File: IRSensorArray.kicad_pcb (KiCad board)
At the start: 2 copper layers, 45 parts, among them J1 EXT_REF, J2 INPUT, J3 PASSTHRU, Q1 DETECT_0, Q2 DETECT_0, Q3 DETECT_0, Q4 DETECT_0, Q5 DETECT_0, Q6 DETECT_0, Q7 DETECT_0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

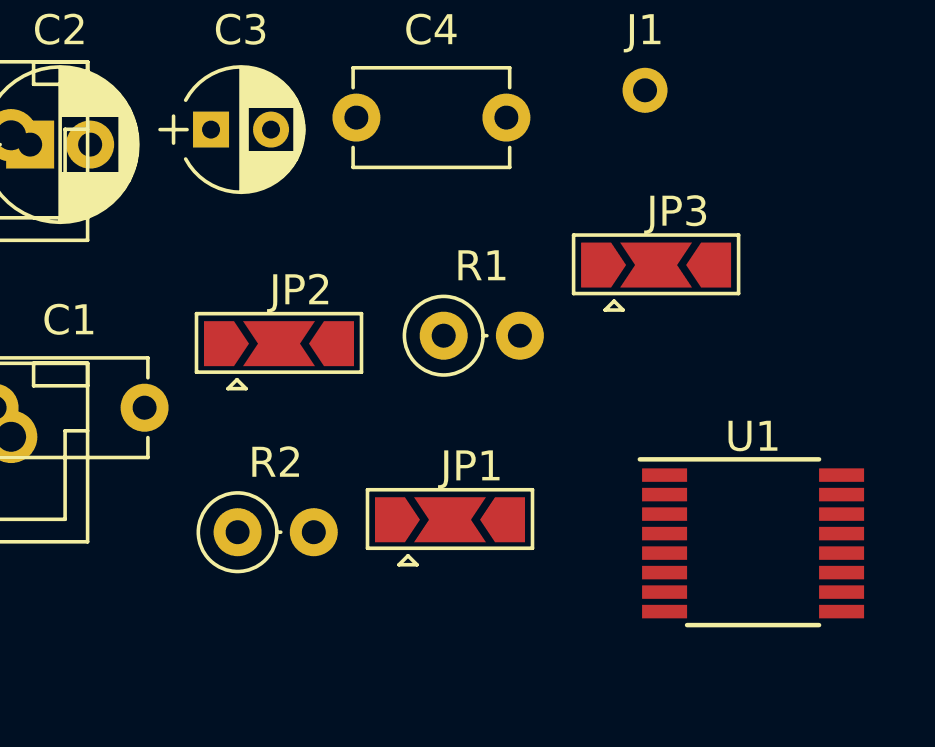
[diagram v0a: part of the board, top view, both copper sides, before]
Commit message: Changed triangle solder bridges to semi-circle
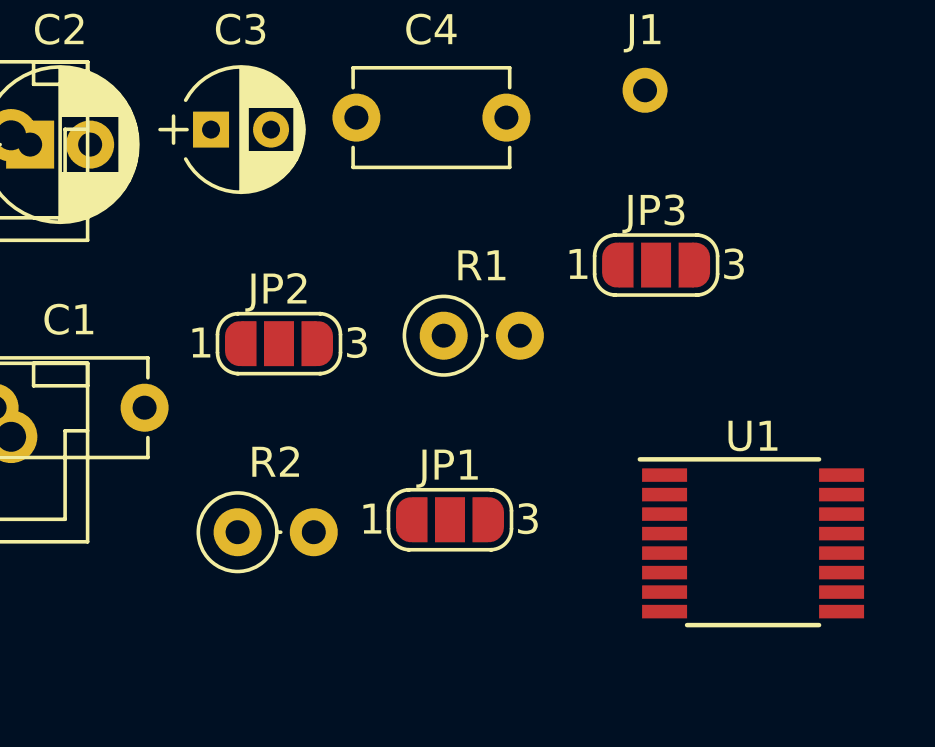
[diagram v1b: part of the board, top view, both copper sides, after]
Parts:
- JP1, JP2, JP3: footprint footprints:SolderJumper-3_P2.0mm_Open_TrianglePad1.0x1.5mm -> footprints:SolderJumper-3_P1.3mm_Open_RoundedPad1.0x1.5mm_NumberLabels

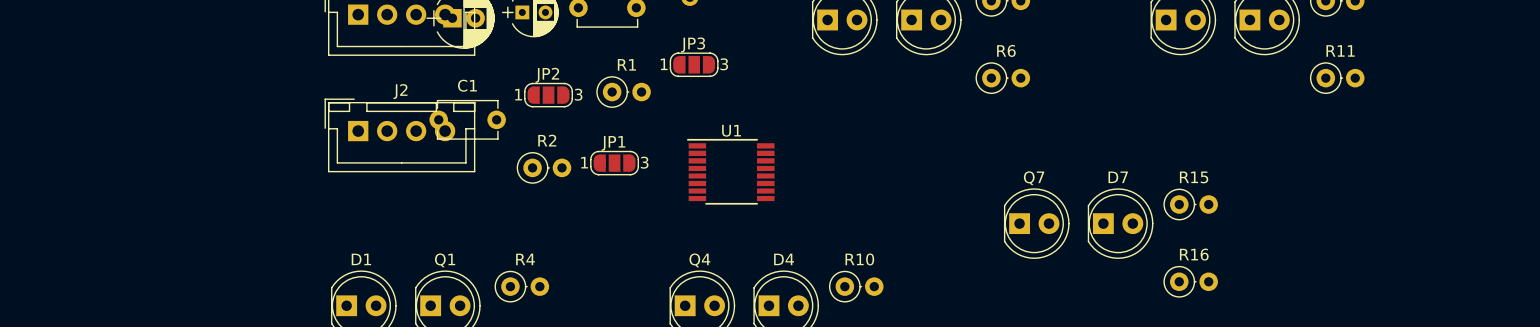
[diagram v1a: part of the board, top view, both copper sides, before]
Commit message: Added mounting holes and some fixes
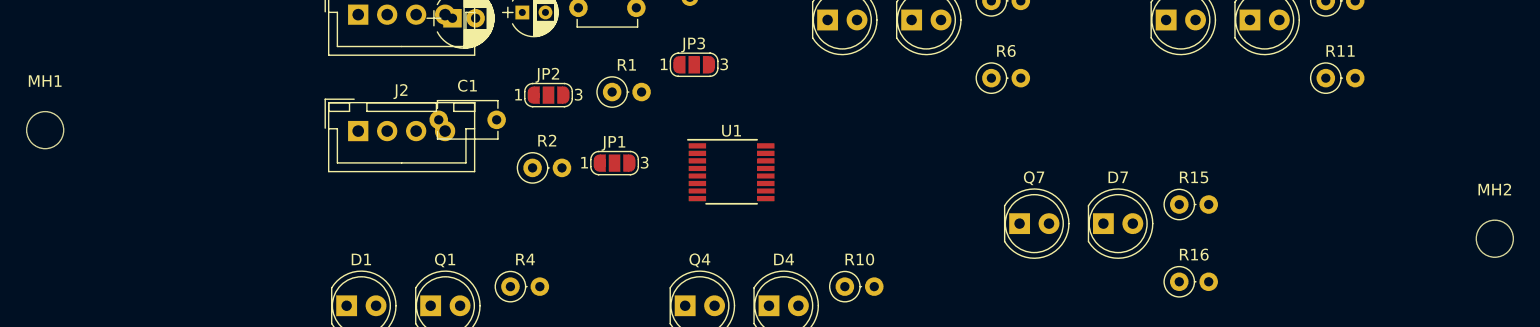
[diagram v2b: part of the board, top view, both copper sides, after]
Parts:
- added MH1: MountingHole_3.2mm_M3, Mounting_Holes:MountingHole_3.2mm_M3, F.Cu at (82.4, 79.9)
- added MH2: MountingHole_3.2mm_M3, Mounting_Holes:MountingHole_3.2mm_M3, F.Cu at (207.5, 89.3)
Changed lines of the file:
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@@
     (tracks 0)
     (zones 0)
-    (modules 45)
+    (modules 47)
     (nets 25)
   )
@@
     (add_net "Net-(D8-Pad2)")
     (add_net "Net-(J1-Pad1)")
+  )
+  (module Mounting_Holes:MountingHole_3.2mm_M3 locked (layer F.Cu)
+    (at 207.518 89.2556)
+    (descr "Mounting Hole 3.2mm, no annular, M3")
+    (tags "mounting hole 3.2mm no annular m3")
+    (attr virtual)
+    (fp_text reference MH2 (at 0 -4.2) (layer F.SilkS)
+      (effects (font (size 1 1) (thickness 0.15)))
+    )
+    (fp_text value MountingHole_3.2mm_M3 (at 0 4.2) (layer F.Fab)
+      (effects (font (size 1 1) (thickness 0.15)))
+    )
+    (fp_circle (center 0 0) (end 3.45 0) (layer F.CrtYd) (width 0.05))
+    (fp_circle (center 0 0) (end 3.2 0) (layer Cmts.User) (width 0.15))
+    (fp_text user %R (at 0.3 0) (layer F.Fab)
+      (effects (font (size 1 1) (thickness 0.15)))
+    )
+    (pad 1 np_thru_hole circle (at 0 0) (size 3.2 3.2) (drill 3.2) (layers *.Cu *.Mask))
   )
   (module Capacitors_THT:C_Disc_D5.1mm_W3.2mm_P5.00mm (layer F.Cu)
@@
       (net 3 +5V))
   )
+  (module Mounting_Holes:MountingHole_3.2mm_M3 locked (layer F.Cu)
+    (at 82.3722 79.883)
+    (descr "Mounting Hole 3.2mm, no annular, M3")
+    (tags "mounting hole 3.2mm no annular m3")
+    (attr virtual)
+    (fp_text reference MH1 (at 0 -4.2) (layer F.SilkS)
+      (effects (font (size 1 1) (thickness 0.15)))
+    )
+    (fp_text value MountingHole_3.2mm_M3 (at 0 4.2) (layer F.Fab)
+      (effects (font (size 1 1) (thickness 0.15)))
+    )
+    (fp_text user %R (at 0.3 0) (layer F.Fab)
+      (effects (font (size 1 1) (thickness 0.15)))
+    )
+    (fp_circle (center 0 0) (end 3.2 0) (layer Cmts.User) (width 0.15))
+    (fp_circle (center 0 0) (end 3.45 0) (layer F.CrtYd) (width 0.05))
+    (pad 1 np_thru_hole circle (at 0 0) (size 3.2 3.2) (drill 3.2) (layers *.Cu *.Mask))
+  )
 )

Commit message: Started PCB layout
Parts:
- Q1, Q2, Q3, Q4, Q5, Q6, Q7, Q8: value DETECT_0 -> DETECT
- moved D1 108.7 mm to (216.9, 102.2)
- moved Q1 108.7 mm to (224.1, 102.2)
- moved R3 108.7 mm to (231.0, 107.2)
- moved R4 108.7 mm to (231.0, 100.5)
- moved R5 98.9 mm to (70.3, 100.2)
- moved R6 98.9 mm to (70.3, 106.9)
- moved D2 98.9 mm to (56.2, 101.9)
- moved Q2 98.9 mm to (63.4, 101.9)
- moved D4 58.7 mm to (86.6, 102.1)
- moved Q4 58.3 mm to (79.7, 102.2)
- moved R10 58.3 mm to (93.5, 100.5)
- moved R9 58.3 mm to (93.5, 107.2)
- moved Q5 35.6 mm to (195.1, 102.1)
- moved R11 35.6 mm to (208.9, 107.1)
- moved R12 35.6 mm to (208.9, 100.5)
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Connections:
- Q1 pad 1: /CH0 -> GND
- Q1 pad 2: GND -> /CH0
- Q2 pad 1: /CH4 -> GND
- Q2 pad 2: GND -> /CH4
- Q3 pad 1: /CH1 -> GND
- Q3 pad 2: GND -> /CH1
- Q4 pad 1: /CH5 -> GND
- Q4 pad 2: GND -> /CH5
- Q5 pad 1: /CH2 -> GND
- Q5 pad 2: GND -> /CH2
- Q6 pad 1: /CH6 -> GND
- Q6 pad 2: GND -> /CH6
- Q7 pad 1: /CH3 -> GND
- Q7 pad 2: GND -> /CH3
- Q8 pad 1: /CH7 -> GND
- Q8 pad 2: GND -> /CH7

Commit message: First draft finished!
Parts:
- removed C3: 1uF, Capacitors_THT:CP_Radial_D4.0mm_P2.00mm
- added G***: LOGO, footprints:rover, B.Cu at (108.2, 127.8)
- J2, J3: moved to B.Cu
- moved R3 122.7 mm to (112.5, 139.2), turned to 90 degrees
- moved R4 122.5 mm to (112.5, 131.6), turned to 270 degrees
- moved Q1 121.7 mm to (106.2, 132.1)
- moved D1 116.6 mm to (106.2, 138.7)
- moved D2 97.8 mm to (146.8, 138.7)
- moved R5 91.5 mm to (153.2, 139.2), turned to 90 degrees
- moved Q2 88.7 mm to (146.8, 132.1)
- moved R6 86.4 mm to (153.2, 131.6), turned to 270 degrees
- moved D5 84.2 mm to (126.5, 138.7)
- moved Q4 82.9 mm to (157.0, 132.1)
- moved R11 82.6 mm to (132.8, 139.2), turned to 90 degrees
- moved R12 82.2 mm to (132.8, 131.6), turned to 270 degrees
- moved D4 79.3 mm to (157.0, 138.7)
- moved R9 76.8 mm to (163.3, 139.2), turned to 90 degrees
- moved R10 76.4 mm to (163.3, 131.6), turned to 270 degrees
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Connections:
- J2 pad 2: /SDA -> /SCL
- J2 pad 3: /SCL -> /SDA
- J3 pad 2: /SDA -> /SCL
- J3 pad 3: /SCL -> /SDA
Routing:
- net +5V: track 0.00 -> 172.3 mm, vias 0 -> 1
- net /SCL: track 0.00 -> 69.1 mm
- net /CH0: track 0.00 -> 56.8 mm
- net /SDA: track 0.00 -> 51.4 mm
- net /CH1: track 0.00 -> 47.9 mm
- net /CH2: track 0.00 -> 38.7 mm
- net /CH3: track 0.00 -> 29.5 mm
- net /CH4: track 0.00 -> 20.2 mm
- net /CH7: track 0.00 -> 18.1 mm
- net /REF: track 0.00 -> 11.3 mm
- net /CH5: track 0.00 -> 11.2 mm
- net /CH6: track 0.00 -> 10.2 mm
- net /SB_0: track 0.00 -> 9.68 mm
- net GND: track 0.00 -> 9.22 mm, vias 0 -> 3
- net /SB_1: track 0.00 -> 8.42 mm
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- added copper zone on B.Cu, net GND
- added copper zone on F.Cu, net GND
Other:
- board outline added: 82.8 x 25.4 mm
- board text added: "EXT_5V"
- board text added: "GND SDA SCL +5V"
- board text added: "INPUT / DAISY-CHAIN"
- board text added: "IR Sensor Array By V2FC"
- board text added: "IREF"
- board text added: "SB0"
- board text added: "SB1"

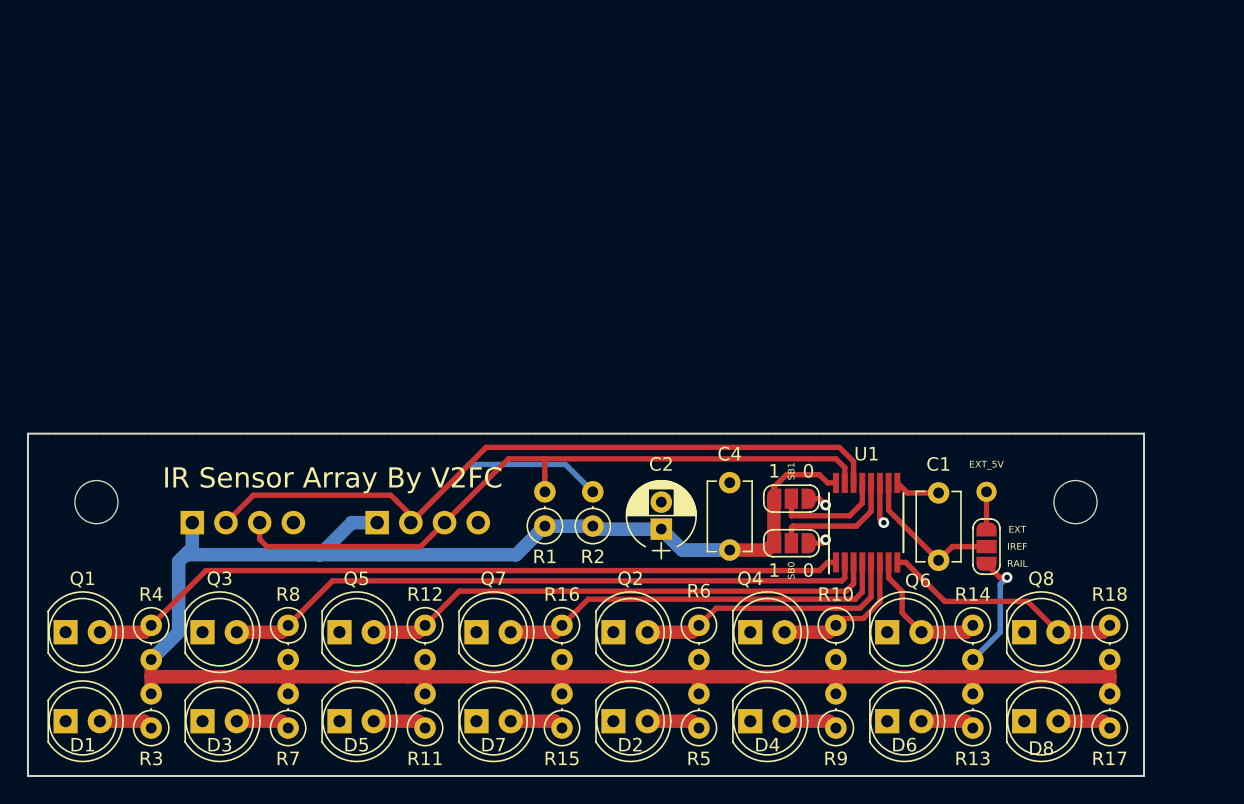
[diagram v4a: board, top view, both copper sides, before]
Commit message: Added images
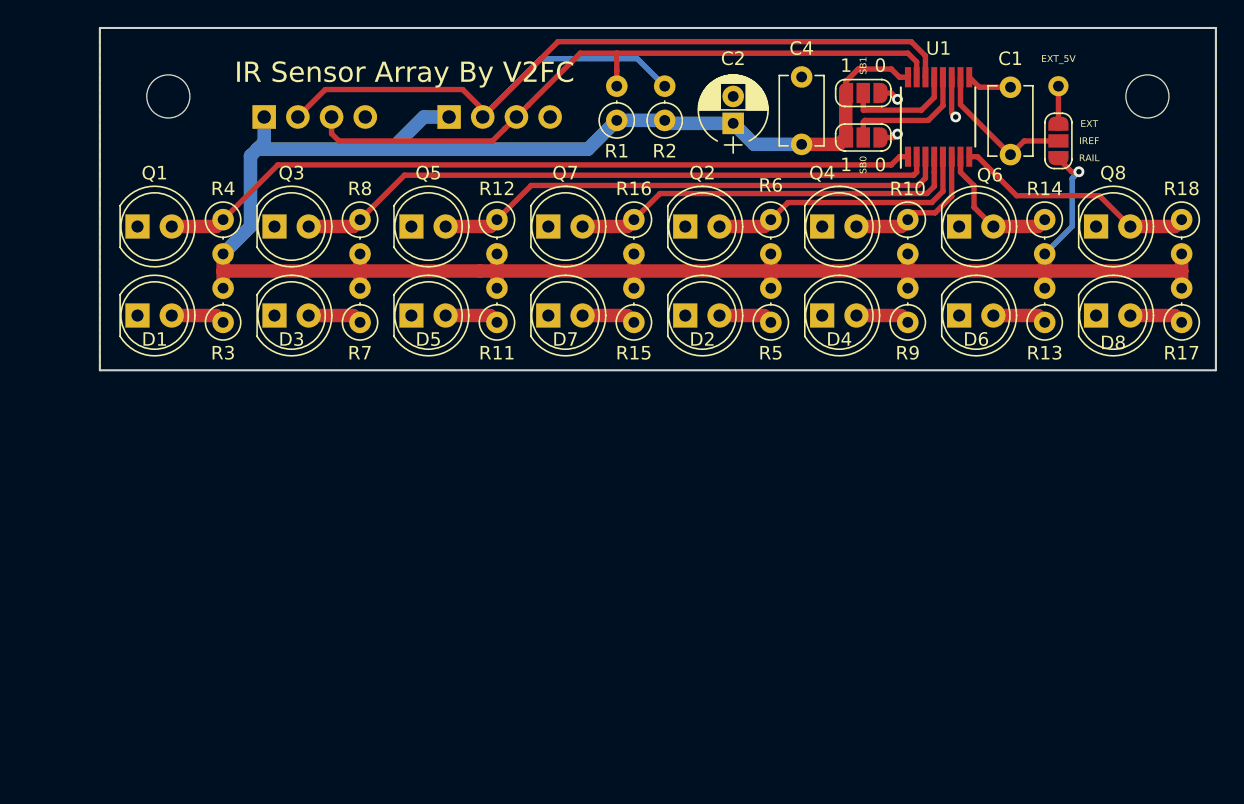
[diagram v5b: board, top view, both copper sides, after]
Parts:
- moved Q1 30.6 mm to (111.5, 102.0)
- moved Q3 30.6 mm to (121.7, 102.0)
- moved Q4 30.6 mm to (162.3, 102.0)
- moved Q5 30.6 mm to (131.8, 102.0)
- moved Q6 30.6 mm to (172.5, 102.0)
- moved Q7 30.6 mm to (142.0, 102.0)
- moved Q8 30.6 mm to (182.6, 102.0)
- moved Q2 30.6 mm to (152.1, 102.0)
- moved C2 30.6 mm to (155.7, 94.3)
- moved D1 30.6 mm to (111.5, 108.6)
- moved D3 30.6 mm to (121.7, 108.6)
- moved D4 30.6 mm to (162.3, 108.6)
- moved D5 30.6 mm to (131.8, 108.6)
- moved D6 30.6 mm to (172.5, 108.6)
- moved D7 30.6 mm to (142.0, 108.6)
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
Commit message: Added library for sensor
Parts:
- Q1, Q2, Q3, Q4, Q5, Q6, Q7, Q8: value DETECT -> QSD124
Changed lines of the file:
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@@
       (outputformat 1)
       (mirror false)
-      (drillshape 1)
+      (drillshape 0)
       (scaleselection 1)
       (outputdirectory ""))
@@
       (effects (font (size 1 1) (thickness 0.15)))
     )
-    (fp_text value DETECT (at 1.27 3.96) (layer F.Fab)
+    (fp_text value QSD124 (at 1.27 3.96) (layer F.Fab)
       (effects (font (size 1 1) (thickness 0.15)))
     )
@@
       (effects (font (size 1 1) (thickness 0.15)))
     )
-    (fp_text value DETECT (at 1.27 3.96) (layer F.Fab)
+    (fp_text value QSD124 (at 1.27 3.96) (layer F.Fab)
       (effects (font (size 1 1) (thickness 0.15)))
     )
@@
       (effects (font (size 1 1) (thickness 0.15)))
     )
-    (fp_text value DETECT (at 1.27 3.96) (layer F.Fab)
+    (fp_text value QSD124 (at 1.27 3.96) (layer F.Fab)
       (effects (font (size 1 1) (thickness 0.15)))
     )
@@
       (effects (font (size 1 1) (thickness 0.15)))
     )
-    (fp_text value DETECT (at 1.27 3.96) (layer F.Fab)
+    (fp_text value QSD124 (at 1.27 3.96) (layer F.Fab)
       (effects (font (size 1 1) (thickness 0.15)))
     )
@@
       (effects (font (size 1 1) (thickness 0.15)))
     )
-    (fp_text value DETECT (at 1.27 3.96) (layer F.Fab)
+    (fp_text value QSD124 (at 1.27 3.96) (layer F.Fab)
       (effects (font (size 1 1) (thickness 0.15)))
     )
@@
       (effects (font (size 1 1) (thickness 0.15)))
     )
-    (fp_text value DETECT (at 1.27 3.96) (layer F.Fab)
+    (fp_text value QSD124 (at 1.27 3.96) (layer F.Fab)
       (effects (font (size 1 1) (thickness 0.15)))
     )
@@
       (effects (font (size 1 1) (thickness 0.15)))
     )
-    (fp_text value DETECT (at 1.27 3.96) (layer F.Fab)
+    (fp_text value QSD124 (at 1.27 3.96) (layer F.Fab)
       (effects (font (size 1 1) (thickness 0.15)))
     )
@@
       (effects (font (size 1 1) (thickness 0.15)))
     )
-    (fp_text value DETECT (at 1.27 3.96) (layer F.Fab)
-      (effects (font (size 1 1) (thickness 0.15)))
-    )
+    (fp_text value QSD124 (at 1.27 3.96) (layer F.Fab)
+      (effects (font (size 1 1) (thickness 0.15)))
+    )

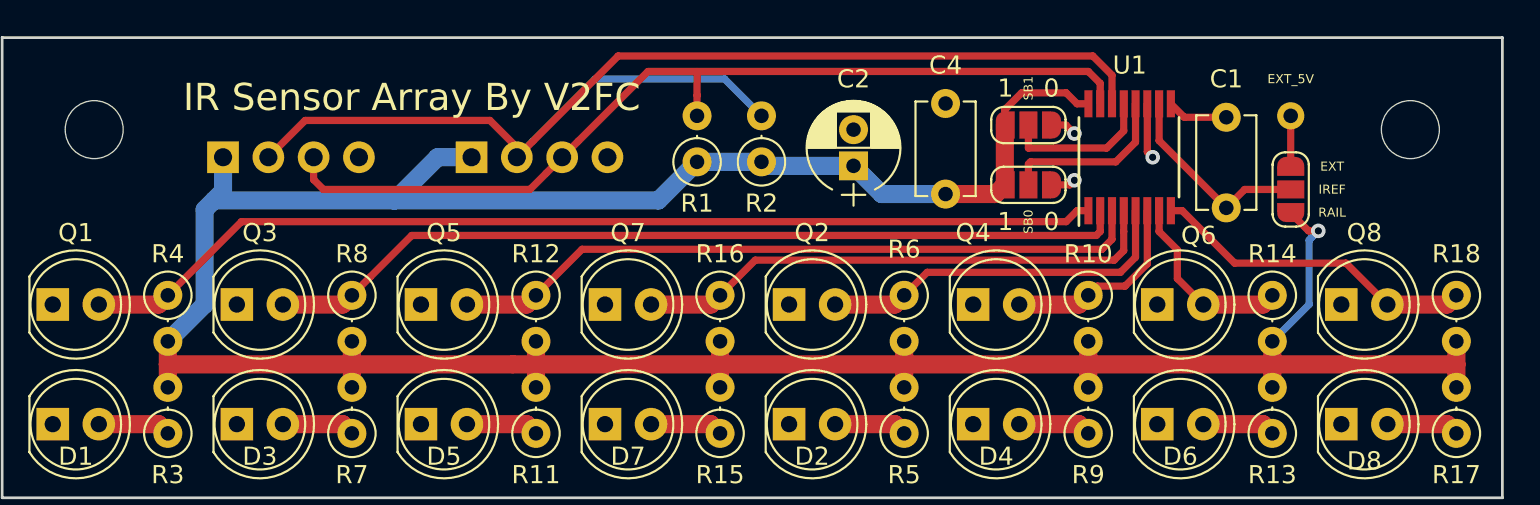
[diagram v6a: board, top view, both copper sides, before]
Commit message: Added reverse voltage diode
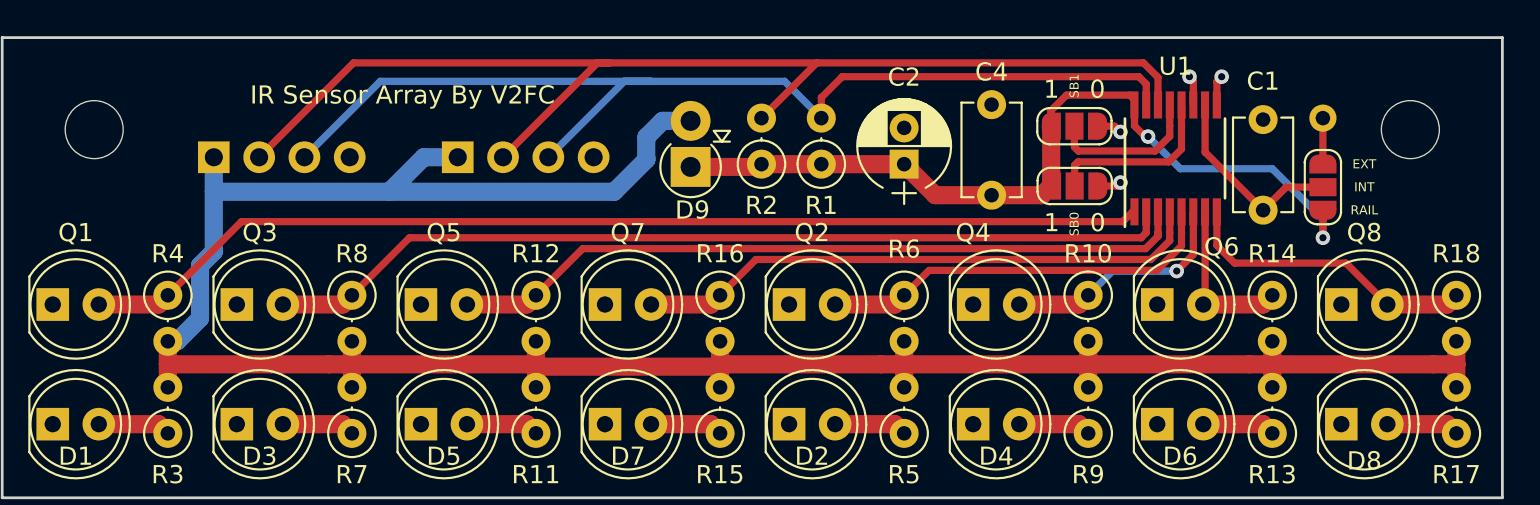
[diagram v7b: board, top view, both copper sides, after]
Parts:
- added D9: 1N4007, Diodes_THT:D_DO-41_SOD81_P2.54mm_Vertical_AnodeUp, F.Cu at (146.7, 94.4)
- D1, D2, D3, D4, D5, D6, D7, D8: value EMITTER -> HSDL-4420
- moved R1 6.86 mm to (153.9, 94.2)
- moved C2 2.80 mm to (158.5, 94.2)
- moved JP1 2.56 mm to (167.9, 95.4)
- moved U1 2.54 mm to (173.5, 93.9)
- moved C4 2.54 mm to (163.3, 95.9)
- moved JP3 2.54 mm to (167.9, 92.1)
- moved C1 2.04 mm to (178.3, 96.8)
- moved J1 1.78 mm to (181.6, 91.7)
- moved JP2 1.78 mm to (181.6, 95.5)
- moved J2 0.76 mm to (133.9, 93.9)
- moved J3 0.51 mm to (120.4, 93.9)
- moved R2 0.13 mm to (150.6, 94.2)
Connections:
- J2 pad 1: +5V -> VCC
- J3 pad 1: +5V -> VCC
- R10 pad 2: +5V -> VCC
- R11 pad 2: +5V -> VCC
- R12 pad 2: +5V -> VCC
- R13 pad 2: +5V -> VCC
- R14 pad 2: +5V -> VCC
- R15 pad 2: +5V -> VCC
- R16 pad 2: +5V -> VCC
- R17 pad 2: +5V -> VCC
- R18 pad 2: +5V -> VCC
- R3 pad 2: +5V -> VCC
- R4 pad 2: +5V -> VCC
- R5 pad 2: +5V -> VCC
- R6 pad 2: +5V -> VCC
- R7 pad 2: +5V -> VCC
- R8 pad 2: +5V -> VCC
- R9 pad 2: +5V -> VCC
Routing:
- net VCC: track 0.00 -> 136.3 mm
- net +5V: track 172.3 -> 46.7 mm, vias 1 -> 2
- net /SDA: track 51.4 -> 59.4 mm
- net GND: track 9.22 -> 5.99 mm, vias 3 -> 4
- net /SCL: track 69.1 -> 66.0 mm
- net /CH1: track 47.9 -> 50.4 mm
- net /CH0: track 56.8 -> 59.3 mm
- net /CH2: track 38.7 -> 41.0 mm
- net /CH5: track 11.2 -> 13.4 mm, vias 0 -> 1
- net /CH3: track 29.5 -> 31.7 mm
- net /CH4: track 20.2 -> 22.3 mm
- net /CH7: track 18.1 -> 16.6 mm
- net /CH6: track 10.2 -> 9.18 mm
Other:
- board text added: "INT"
- board text removed: "EXT_5V"
- board text removed: "IREF"
